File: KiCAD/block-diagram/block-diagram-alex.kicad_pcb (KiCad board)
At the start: 4 copper layers, 50.8 x 38.1 mm, 33 parts, among them J1 Conn_01x08, J2 Conn_01x08, J3 Conn_01x10, Q3 NMOS, Q4 NMOS, U1 74LS02, U3 74LS11, U6 LMC555xM

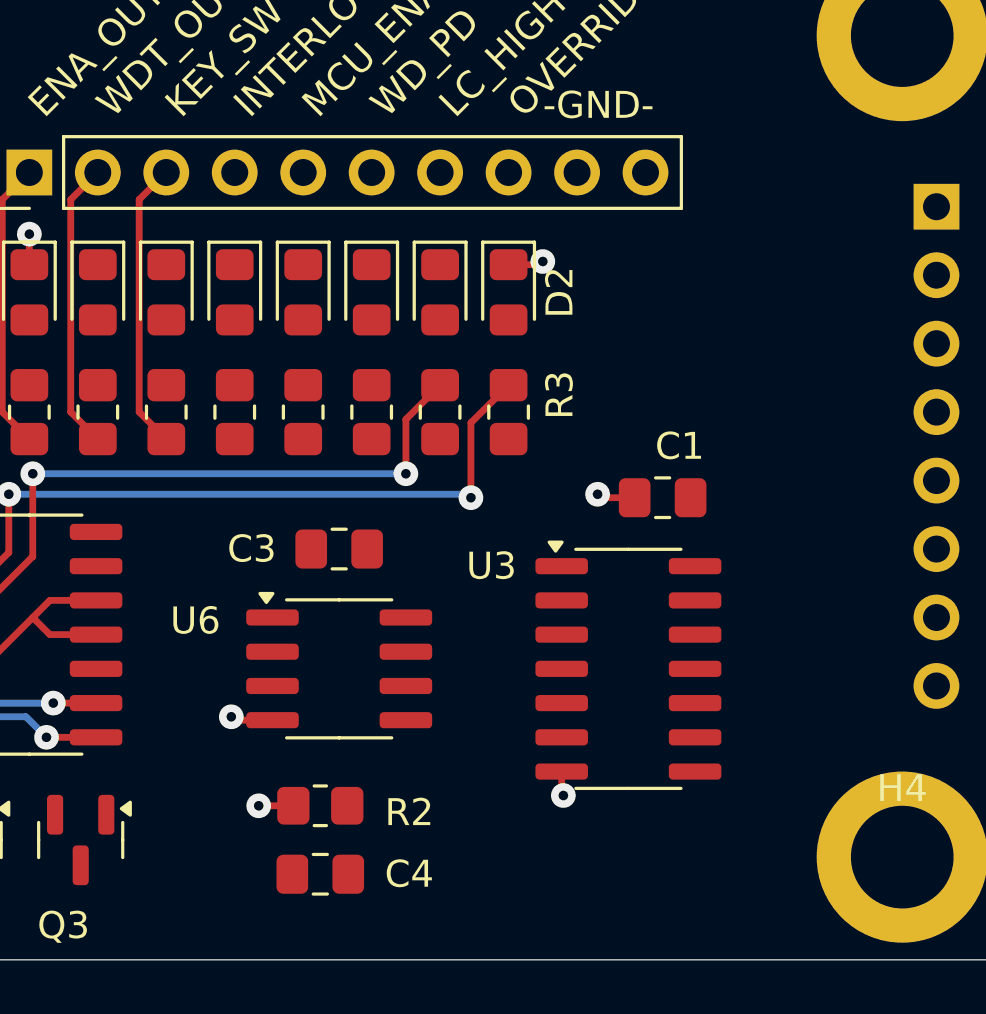
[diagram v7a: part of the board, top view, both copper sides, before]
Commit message: Potentiometer
I added the potentiometer to modulate the watchdog time constant.
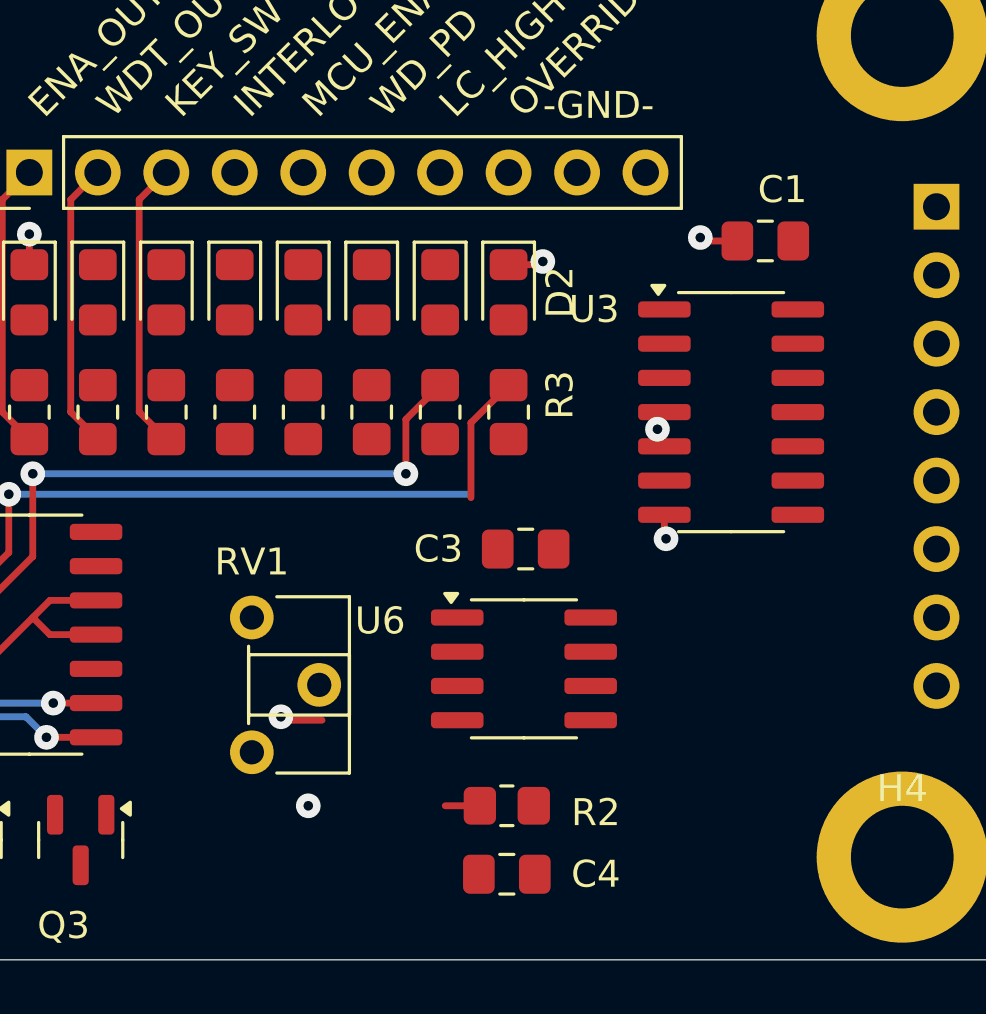
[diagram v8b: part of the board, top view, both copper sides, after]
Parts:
- added RV1: R_Potentiometer_US, Potentiometer_THT:Potentiometer_ACP_CA6-H2,5_Horizontal, F.Cu at (142.2, 96.5)
- moved C1 10.3 mm to (161.3, 82.5)
- moved U3 10.3 mm to (160.0, 88.9)
- moved C3 6.92 mm to (152.4, 94.0)
- moved C4 6.92 mm to (151.7, 106.0)
- moved R2 6.92 mm to (151.7, 103.5)
- moved U6 6.86 mm to (152.3, 98.4)
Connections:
- R2 pad 1: +5V -> Net-(R2-Pad1)
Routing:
- net Net-(R2-Pad1): track 0.00 -> 1.29 mm, vias 0 -> 1
- net +5V: track 2.87 -> 1.58 mm, vias 2 -> 1
- net GND: track 21.2 -> 21.4 mm, vias 6 -> 7
- net /OVERRIDE: track 26.0 -> 25.9 mm, vias 2 -> 1
